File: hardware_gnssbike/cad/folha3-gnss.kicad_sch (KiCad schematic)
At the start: 10 parts, among them J302 contato de mola, 2 vias, U301 u-blox MAX-F10S, U302 TI TXU0204BQAR

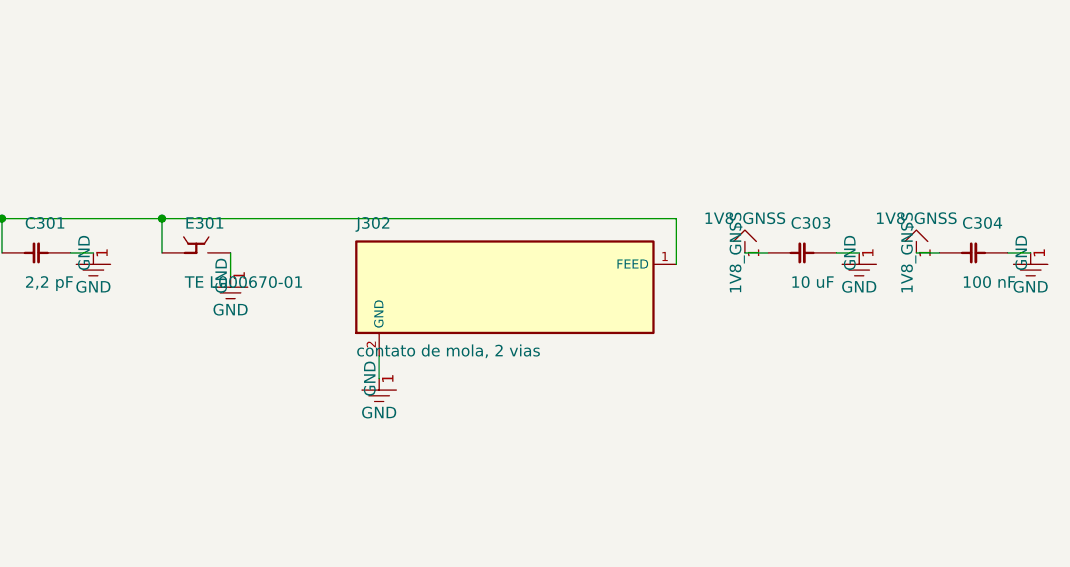
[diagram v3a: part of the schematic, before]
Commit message: feat(hardware): a u.FL for the GNSS antenna, and an assembly drawing that reads
The GNSS antenna arrived on a spring contact. The line it feeds is the
L1 + L5 path of the MAX-F10S and section 4.4 of the integration manual asks
for 50 ohm on ALL of it - and a pair of gold pads that a leaf spring presses
on has no defined impedance at 1.2 and 1.6 GHz, no defined return path, and
a contact resistance that changes with how the case was closed. J302 is a
Hirose U.FL-R-SMT-1 now, the 50 ohm coaxial transition every GNSS module
reference design uses for an external element. It costs 2.6 x 2.6 mm of
board and trades a mechanical fit for a cable, which is a mechanical
decision that was recorded nowhere. The RF path went from 8.2 to 5.7 mm.
The three solar spring contacts stay spring contacts: no RF there.

And the assembly drawing stopped coming out of a KiCad layer, because
neither layer can give one for this board. Silkscreen is silkscreen: it
obeys manufacturing, 0.6 mm of text, and 127 designators on a 34 x 90 mm
board at 48% occupancy do not fit around the parts without landing on one
another or drifting so far from the part that they name nothing. F.Fab
carries whatever each library footprint put there, at whatever size its
author chose, plus the value - "TP110" at 1.0 mm beside "100 nF" at 0.5,
both over the outline.

An assembly drawing is not a copper layer. It is a drawing, and it may do
the one thing a silkscreen may not: put the label where it can be read and
draw a LINE from the label to the part. montagem.py does that - the
reference inside the courtyard where it fits, outside with a dot and a
leader where it does not. 92 of the 127 need the leader.

The silkscreen placement was also backwards: it preferred a spot clear of
ANY part's outline to a spot near its own, which on a board this dense
pushes the designator millimetres away and produces a cloud where nothing
points at anything. Proximity decides now - nearest first, the first
candidate that misses every 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
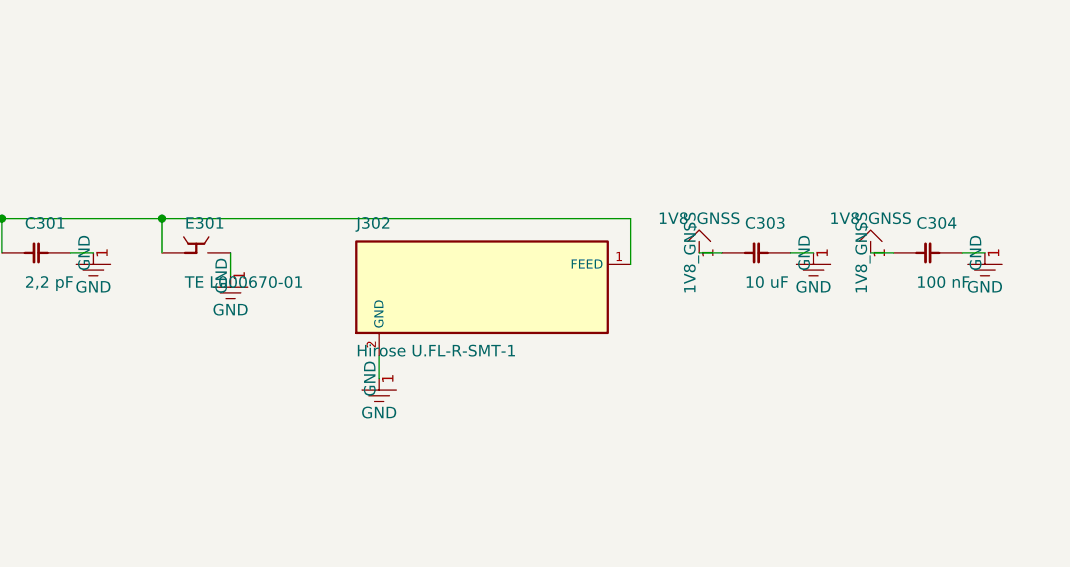
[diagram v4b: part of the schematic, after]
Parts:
- J302: value contato de mola, 2 vias -> Hirose U.FL-R-SMT-1; footprint gnssbike:ContatoMola_2x2mm_P3mm -> Connector_Coaxial:U.FL_Hirose_U.FL-R-SMT-1_Vertical
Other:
- moved on the sheet: C303, C304, J302
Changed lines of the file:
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@@
 	(wire
 		(pts
-			(xy 242.570 35.560) (xy 245.110 35.560)
-		)
-		(stroke (width 0) (type default))
-	)
-	(wire
-		(pts
-			(xy 261.620 35.560) (xy 264.160 35.560)
+			(xy 237.490 35.560) (xy 240.030 35.560)
+		)
+		(stroke (width 0) (type default))
+	)
+	(wire
+		(pts
+			(xy 256.540 35.560) (xy 259.080 35.560)
 		)
 		(stroke (width 0) (type default))
@@
 	(wire
 		(pts
-			(xy 234.950 35.560) (xy 232.410 35.560)
-		)
-		(stroke (width 0) (type default))
-	)
-	(wire
-		(pts
-			(xy 254.000 35.560) (xy 251.460 35.560)
+			(xy 229.870 35.560) (xy 227.330 35.560)
+		)
+		(stroke (width 0) (type default))
+	)
+	(wire
+		(pts
+			(xy 248.920 35.560) (xy 246.380 35.560)
 		)
 		(stroke (width 0) (type default))
@@
 	(wire
 		(pts
-			(xy 224.790 31.750) (xy 224.790 36.830)
-		)
-		(stroke (width 0) (type default))
-	)
-	(wire
-		(pts
-			(xy 167.640 31.750) (xy 224.790 31.750)
+			(xy 219.710 31.750) (xy 219.710 36.830)
+		)
+		(stroke (width 0) (type default))
+	)
+	(wire
+		(pts
+			(xy 167.640 31.750) (xy 219.710 31.750)
 		)
 		(stroke (width 0) (type default))
@@
 	(symbol
 		(lib_id "gnssbike:J302")
-		(at 205.740 39.370 0)
+		(at 203.200 39.370 0)
 		(unit 1)
 		(exclude_from_sim no)
@@
 			(effects (font (size 1.27 1.27)) (justify left bottom))
 		)
-		(property "Value" "contato de mola, 2 vias"
+		(property "Value" "Hirose U.FL-R-SMT-1"
 			(at 189.230 45.720 0)
 			(effects (font (size 1.27 1.27)) (justify left top))
 		)
-		(property "Footprint" "gnssbike:ContatoMola_2x2mm_P3mm"
-			(at 205.74 39.37 0)
-			(effects (font (size 1.27 1.27)) (hide yes))
-		)
-		(property "Datasheet" ""
-			(at 205.74 39.37 0)
-			(effects (font (size 1.27 1.27)) (hide yes))
-		)
-		(property "Description" "onde a antena da parede da caixa encosta na placa. 04:271 decidiu contatos de mola e 04:661 registrava que a area deles nao estava dimensionada; sao dois pads de 2,0 x 2,0 mm a 3,0 mm de passo, sem pasta. CONFERIR a mola escolhida antes de fabricar | PINAGEM NAO CONFIRMADA NA FICHA"
-			(at 205.74 39.37 0)
+		(property "Footprint" "Connector_Coaxial:U.FL_Hirose_U.FL-R-SMT-1_Vertical"
+			(at 203.2 39.37 0)
+			(effects (font (size 1.27 1.27)) (hide yes))
+		)
+		(property "Datasheet" ""
+			(at 203.2 39.37 0)
+			(effects (font (size 1.27 1.27)) (hide yes))
+		)
+		(property "Description" "conector coaxial u.FL da antena GNSS L1+L5. Substitui o contato de mola que 04:271 tinha decidido: mola nao tem impedancia definida, e a 4.4 do manual do MAX-F10S pede 50 ohm em TODO o caminho de RF. CONFERIR o cabo e o conector da outra ponta antes de fabricar | PINAGEM NAO CONFIRMADA NA FICHA"
+			(at 203.2 39.37 0)
 			(effects (font (size 1.27 1.27)) (hide yes))
 		)
@@
 	(symbol
 		(lib_id "gnssbike:C303")
-		(at 238.760 35.560 0)
+		(at 233.680 35.560 0)
 		(unit 1)
 		(exclude_from_sim no)
@@
 		(dnp no)
 		(property "Reference" "C303"
-			(at 237.490 33.020 0)
+			(at 232.410 33.020 0)
 			(effects (font (size 1.27 1.27)) (justify left bottom))
 		)
 		(property "Value" "10 uF"
-			(at 237.490 38.100 0)
+			(at 232.410 38.100 0)
 			(effects (font (size 1.27 1.27)) (justify left top))
 		)
 		(property "Footprint" "Capacitor_SMD:C_0603_1608Metric"
-			(at 238.76 35.56 0)
-			(effects (font (size 1.27 1.27)) (hide yes))
-		)
-		(property "Datasheet" ""
-			(at 238.76 35.56 0)
+			(at 233.68 35.56 0)
+			(effects (font (size 1.27 1.27)) (hide yes))
+		)
+		(property "Datasheet" ""
+			(at 233.68 35.56 0)
 			(effects (font (size 1.27 1.27)) (hide yes))
 		)
 		(property "Description" ""
-			(at 238.76 35.56 0)
+			(at 233.68 35.56 0)
 			(effects (font (size 1.27 1.27)) (hide yes))
 		)
@@
 	(symbol
 		(lib_id "gnssbike:C304")
-		(at 257.810 35.560 0)
+		(at 252.730 35.560 0)
 		(unit 1)
 		(exclude_from_sim no)
@@
 		(dnp no)
 		(property "Reference" "C304"
-			(at 256.540 33.020 0)
+			(at 251.460 33.020 0)
 			(effects (font (size 1.27 1.27)) (justify left bottom))
 		)
 		(property "Value" "100 nF"
-			(at 256.540 38.100 0)
+			(at 251.460 38.100 0)
 			(effects (font (size 1.27 1.27)) (justify left top))
 		)
 		(property "Footprint" "Capacitor_SMD:C_0402_1005Metric"
-			(at 257.81 35.56 0)
-			(effects (font (size 1.27 1.27)) (hide yes))
-		)
-		(property "Datasheet" ""
-			(at 257.81 35.56 0)
+			(at 252.73 35.56 0)
+			(effects (font (size 1.27 1.27)) (hide yes))
+		)
+		(property "Datasheet" ""
+			(at 252.73 35.56 0)
 			(effects (font (size 1.27 1.27)) (hide yes))
 		)
 		(property "Description" ""
-			(at 257.81 35.56 0)
+			(at 252.73 35.56 0)
 			(effects (font (size 1.27 1.27)) (hide yes))
 		)
@@
 	(symbol
 		(lib_id "power:GND")
-		(at 245.110 35.560 0)
+		(at 240.030 35.560 0)
 		(unit 1)
 		(exclude_from_sim no)
@@
 		(dnp no)
 		(property "Reference" "#PWR010"
-			(at 245.10999999999999 35.56 0)
+			(at 240.03 35.56 0)
 			(effects (font (size 1.27 1.27)) (hide yes))
 		)
 		(property "Value" "GND"
-			(at 245.110 39.370 0)
-			(effects (font (size 1.27 1.27)))
-		)
-		(property "Footprint" ""
-			(at 245.10999999999999 35.56 0)
-			(effects (font (size 1.27 1.27)) (hide yes))
-		)
-		(property "Datasheet" ""
-			(at 245.10999999999999 35.56 0)
+			(at 240.030 39.370 0)
+			(effects (font (size 1.27 1.27)))
+		)
+		(property "Footprint" ""
+			(at 240.03 35.56 0)
+			(effects (font (size 1.27 1.27)) (hide yes))
+		)
+		(property "Datasheet" ""
+			(at 240.03 35.56 0)
 			(effects (font (size 1.27 1.27)) (hide yes))
 		)
@@
 	(symbol
 		(lib_id "power:GND")
-		(at 264.160 35.560 0)
+		(at 259.080 35.560 0)
 		(unit 1)
 		(exclude_from_sim no)
@@
 		(dnp no)
 		(property "Reference" "#PWR011"
-			(at 264.16 35.56 0)
+			(at 259.08000000000004 35.56 0)
 			(effects (font (size 1.27 1.27)) (hide yes))
 		)
 		(property "Value" "GND"
-			(at 264.160 39.370 0)
-			(effects (font (size 1.27 1.27)))
-		)
-		(property "Footprint" ""
-			(at 264.16 35.56 0)
-			(effects (font (size 1.27 1.27)) (hide yes))
-		)
-		(property "Datasheet" ""
-			(at 264.16 35.56 0)
+			(at 259.080 39.370 0)
+			(effects (font (size 1.27 1.27)))
+		)
+		(property "Footprint" ""
+			(at 259.08000000000004 35.56 0)
+			(effects (font (size 1.27 1.27)) (hide yes))
+		)
+		(property "Datasheet" ""
+			(at 259.08000000000004 35.56 0)
 			(effects (font (size 1.27 1.27)) (hide yes))
 		)
@@
 	(symbol
 		(lib_id "power:1V8_GNSS")
-		(at 232.410 35.560 0)
+		(at 227.330 35.560 0)
 		(unit 1)
 		(exclude_from_sim no)
@@
 		(dnp no)
 		(property "Reference" "#PWR018"
-			(at 232.41 35.56 0)
+			(at 227.33 35.56 0)
 			(effects (font (size 1.27 1.27)) (hide yes))
 		)
 		(property "Value" "1V8_GNSS"
-			(at 232.410 31.750 0)
-			(effects (font (size 1.27 1.27)))
-		)
-		(property "Footprint" ""
-			(at 232.41 35.56 0)
-			(effects (font (size 1.27 1.27)) (hide yes))
-		)
-		(property "Datasheet" ""
-			(at 232.41 35.56 0)
+			(at 227.330 31.750 0)
+			(effects (font (size 1.27 1.27)))
+		)
+		(property "Footprint" ""
+			(at 227.33 35.56 0)
+			(effects (font (size 1.27 1.27)) (hide yes))
+		)
+		(property "Datasheet" ""
+			(at 227.33 35.56 0)
 			(effects (font (size 1.27 1.27)) (hide yes))
 		)
@@
 	(symbol
 		(lib_id "power:1V8_GNSS")
-		(at 251.460 35.560 0)
+		(at 246.380 35.560 0)
 		(unit 1)
 		(exclude_from_sim no)
@@
 		(dnp no)
 		(property "Reference" "#PWR019"
-			(at 251.46 35.56 0)
+			(at 246.38 35.56 0)
 			(effects (font (size 1.27 1.27)) (hide yes))
 		)
 		(property "Value" "1V8_GNSS"
-			(at 251.460 31.750 0)
-			(effects (font (size 1.27 1.27)))
-		)
-		(property "Footprint" ""
-			(at 251.46 35.56 0)
-			(effects (font (size 1.27 1.27)) (hide yes))
-		)
-		(property "Datasheet" ""
-			(at 251.46 35.56 0)
-			(effects (font (size 1.27 1.27)) (hide yes))
-		)
+			(at 246.380 31.750 0)
+			(effects (font (size 1.27 1.27)))
+		)
+		(property "Footprint" ""
+			(at 246.38 35.56 0)
+			(effects (font (size 1.27 1.27)) (hide yes))
+		)
+		(property "Datasheet" ""
+			(at 246.38 35.56 0)
+			(effects (font (size 1.27 1.27)) (hide yes))
+		)

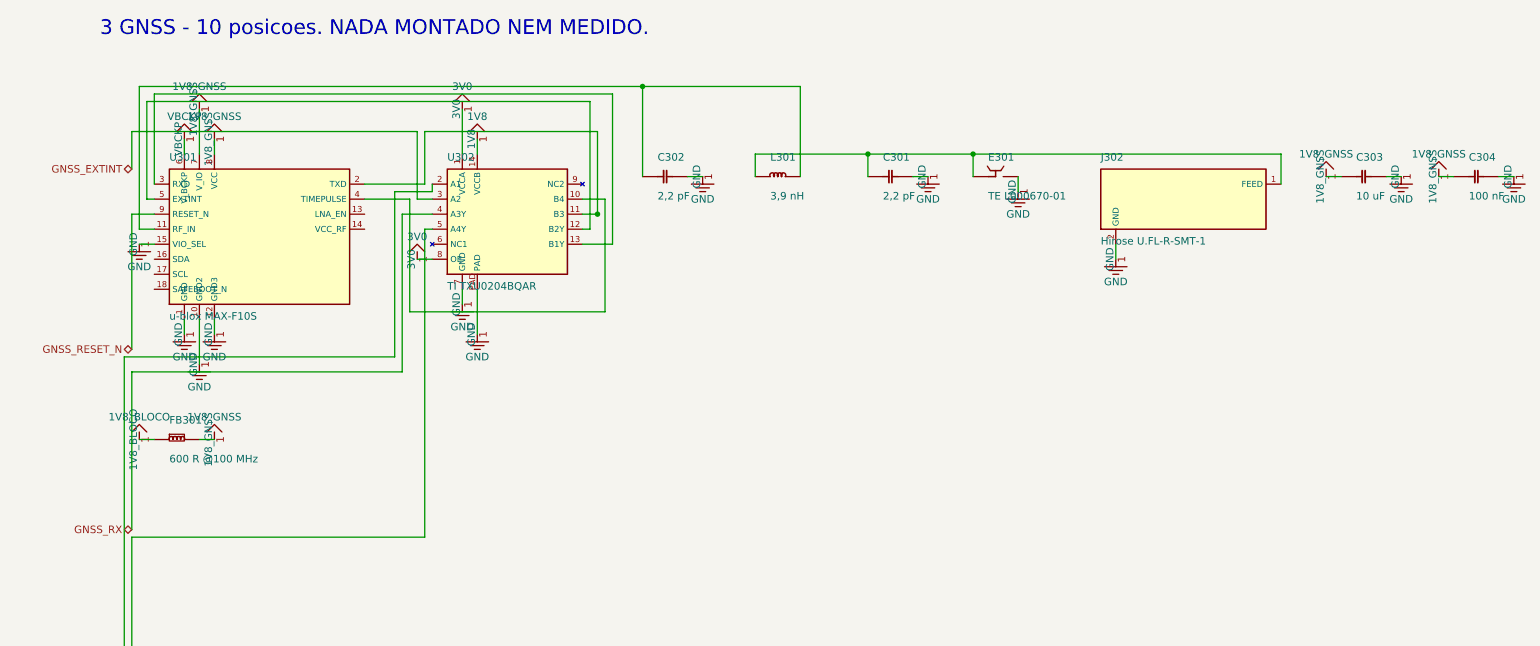
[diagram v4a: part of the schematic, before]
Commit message: feat(hardware): buy what JLCPCB can actually assemble
The board is made and assembled at JLCPCB, so every part has to be one
LCSC stocks - the owner's rule of 2026-09-24, with the Minew module and
the solar cells as the only exceptions. Three surveys against LCSC's
catalogue and JLCPCB's assembly API checked the 34 parts that are not a
plain resistor or capacitor, and this is what came back.

Parts that changed, and what each change costs:

  J101  Molex 2036150003 -> HRO TYPE-C-31-M-12 (C165948). 309 in the
        world at US$ 5,69 against 91.943 at US$ 0,186, and KiCad carries
        the land pattern under the part's own name. The body goes from
        8,58 to 7,35 mm, so the case opening changes.
  D101  ESD761DPYR -> TPD1E05U06DPYR (C436349). Same X1SON-2 and better
        capacitance, but bidirectional 24 V becomes unidirectional
        5,5 V: orientation now matters and a faulty cable putting 20 V
        on a CC line is no longer survivable.
  J103  three pairs of spring pads -> one JST ZH of 4 ways, with three
        0 ohm joining the groups to SRC. Nobody assembles a spring, a
        bicycle vibrates, and a pressed contact that opens and closes on
        the input of a switching converter is a dirty transient. ZH of
        1,5 mm on purpose: the cell is a GH of 1,25 and 4,2 V into the
        harvester's 2,73 V input would kill it. The 0 ohm let one face
        be measured alone in the sun.
  D105  new: a clamp on SRC. The right connector stops the mistake; the
        clamp stops the damage when the mistake comes from a crimp.
  J101  the shell had no pin, so four pads of the land pattern floated.

U101 and U103 stay as they are and go by consignment: the nPM1300 QFN is
zero on both sides and the whole e-peas line is zero. The nPM1300 does
exist in WLCSP-35, but its 0,419 x 0,440 mm ball pitch is smaller than
this board's 0,45 mm via and would force via-in-pad on every board ever
made, probably six layers, twice the thermal resistance and a light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
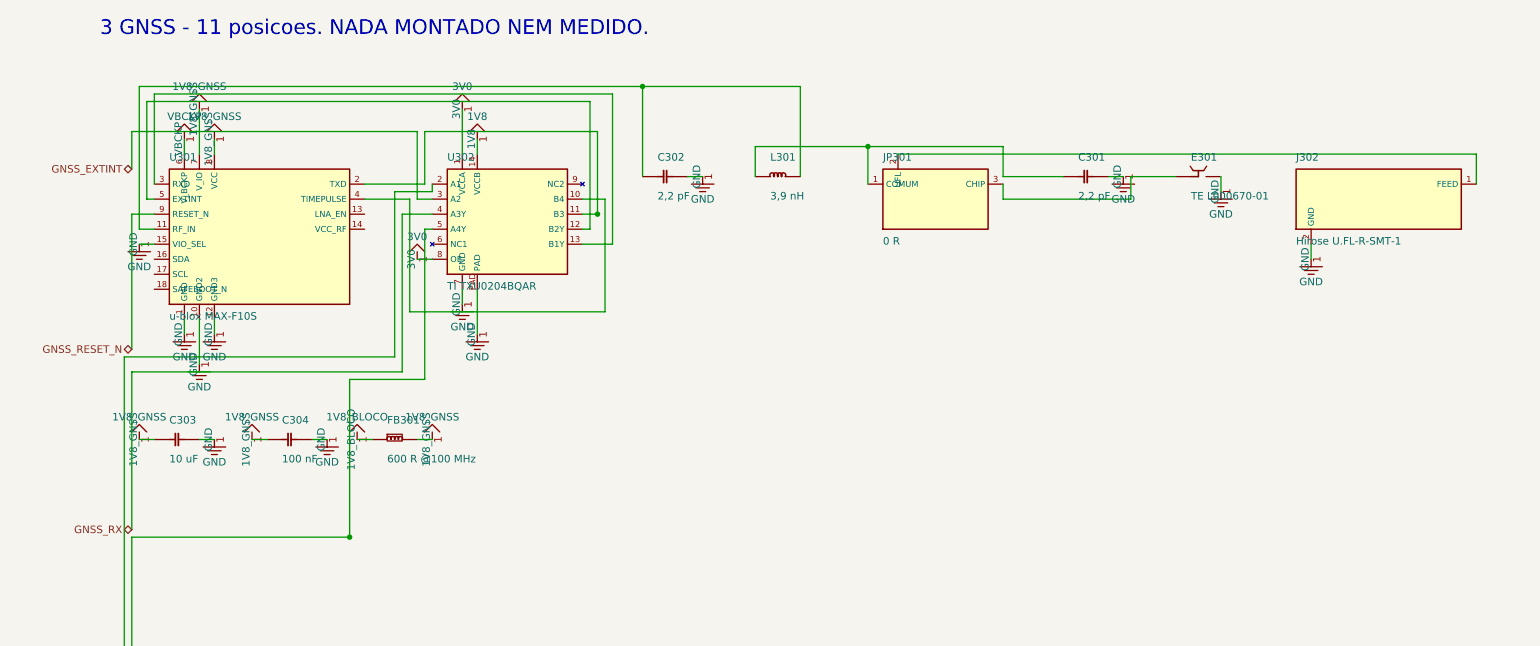
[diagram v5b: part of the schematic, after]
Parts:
- added JP301: 0 R, gnssbike:JumperRF_3x0402, symbol gnssbike:JP301
- U301: footprint gnssbike:u-blox_MAX-F10S_9.7x10.1mm -> gnssbike:u-blox_MAX_LCC-18_9.7x10.1mm
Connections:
- net at C301.1, L301.1: now also JP301.1 (COMUM); no longer E301.1 (FEED), J302.1 (FEED)
- new net: E301.1 (FEED), JP301.3 (CHIP)
- new net: J302.1 (FEED), JP301.2 (UFL)
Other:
- note added: "3 GNSS - 11 posicoes. NADA MONTADO NEM MEDIDO."
- note removed: "3 GNSS - 10 posicoes. NADA MONTADO NEM MEDIDO."
- moved on the sheet: C301, C303, C304, E301, FB301, J302

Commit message: feat(hardware): the GNSS antenna comes onto the board, and the cut-out shrinks
The TE L000670-01 is zero at LCSC, and it was never going to work here
anyway: it asked for 40,5 x 14,5 mm with no copper on ANY layer, which is
wider than this whole 34 mm board, and its own efficiency curve collapsed
with a short ground plane - 62 % in L5 at 90 mm of ground, 43 % at 70,
29 % at 50. L5 is the entire reason the MAX-F10S was chosen.

The Unictron H2UJ4U1H2Q0100 (C6569550, 5.491 in stock) replaces it. Its
cut-out is 15,00 x 9,35 mm on the top layer and 15,00 x 9,88 on the
bottom, measured from the BOARD EDGE, and the part is 5,0 x 3,0 x 0,5 mm
against 14 x 10,75 x 1.

E301 was the only part still living outside the board: it had no
footprint, so the jumper's CHIP branch went to something that was not
laid out. It now has a land pattern read off the layout guide - two
ground/tuning pads of 0,80 x 2,98 straddling the ends, 0,40 under the
body and 0,40 outside for the fillet to climb the wrap-around
metallisation, and a 1,00 x 2,00 signal pad at the geometric centre -
and it sits on the bottom edge, 0,30 mm from it.

Its two end pads are ground AND tuning: they reach the plane through
C305 and C306, positions [8] and [9] of the data sheet's network, not
directly. The matching network's values changed with the antenna: the
shunt is 1,5 pF, the series element becomes a 3,6 pF CAPACITOR instead
of a 3,9 nH inductor, and the second shunt is not fitted. Same 0402
land patterns, so the board does not change - only what is soldered on
it, and it changes again if the u.FL branch is the one fitted.

The cut-out is 20,08 mm wide and not the data sheet's 15,00, and that is
deliberate: the cut-out is asymmetric about the antenna - 2,46 mm one
side and 7,54 the other - and which side is which is not determined.
Applying 7,54 to both sides meets the requirement whichever way the part
faces. It costs about 5 mm of ground plane on an antenna that depends on
it, and it can go back to 15,00 onc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
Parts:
- added C305: 2,7 pF, Resistor_SMD:R_0402_1005Metric, symbol gnssbike:C305
- added C306: 6,8 pF, Resistor_SMD:R_0402_1005Metric, symbol gnssbike:C306
- C301: value 2,2 pF -> 1,5 pF
- C302: value 2,2 pF -> NP
- E301: value TE L000670-01 -> Unictron H2UJ4U1H2Q0100; footprint (none) -> gnssbike:Antena_Unictron_H2UJ4U1H2Q0100_5x3mm
- L301: value 3,9 nH -> 3,6 pF
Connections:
- net GND: now also C305.2, C306.2; no longer E301.2 (GND)
- net at E301.1 (GND_T1): now also C305.1; no longer JP301.3 (CHIP)
- new net: C306.1, E301.2 (GND_T2)
- new net: E301.3 (FEED), JP301.3 (CHIP)
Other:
- note added: "3 GNSS - 13 posicoes. NADA MONTADO NEM MEDIDO."
- note removed: "3 GNSS - 11 posicoes. NADA MONTADO NEM MEDIDO."
- moved on the sheet: C303, C304, FB301, J302
